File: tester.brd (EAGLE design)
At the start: 56 x 67 mm, 71 parts, among them IC1 ATmega8/88/168, K1 NA 05W K, M1 SP6000C-180, P1 250, P2 10k lin, Q1 BC847CSMD, Q2 BC847CSMD, Q3 BC328-40, Q4 8,000 MHz, Q5 BC847CSMD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

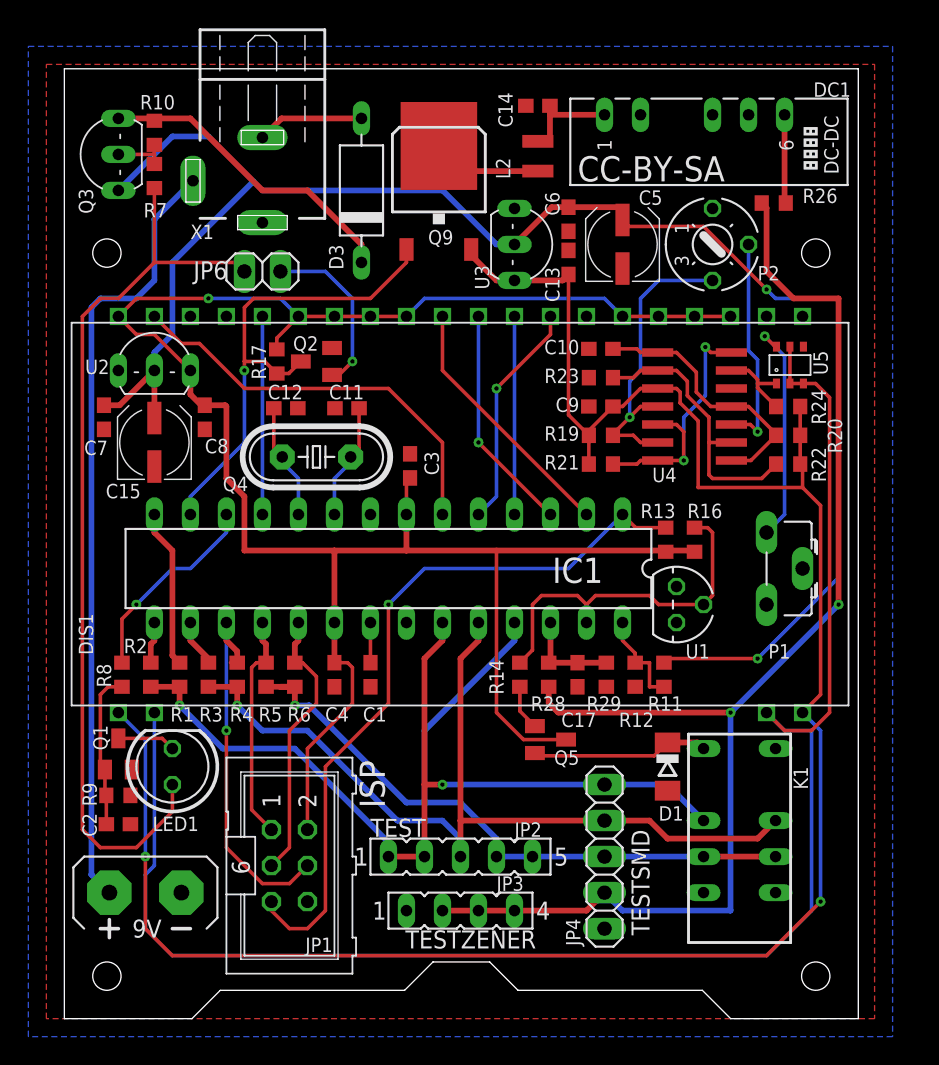
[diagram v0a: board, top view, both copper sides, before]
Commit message: rearranged top mask
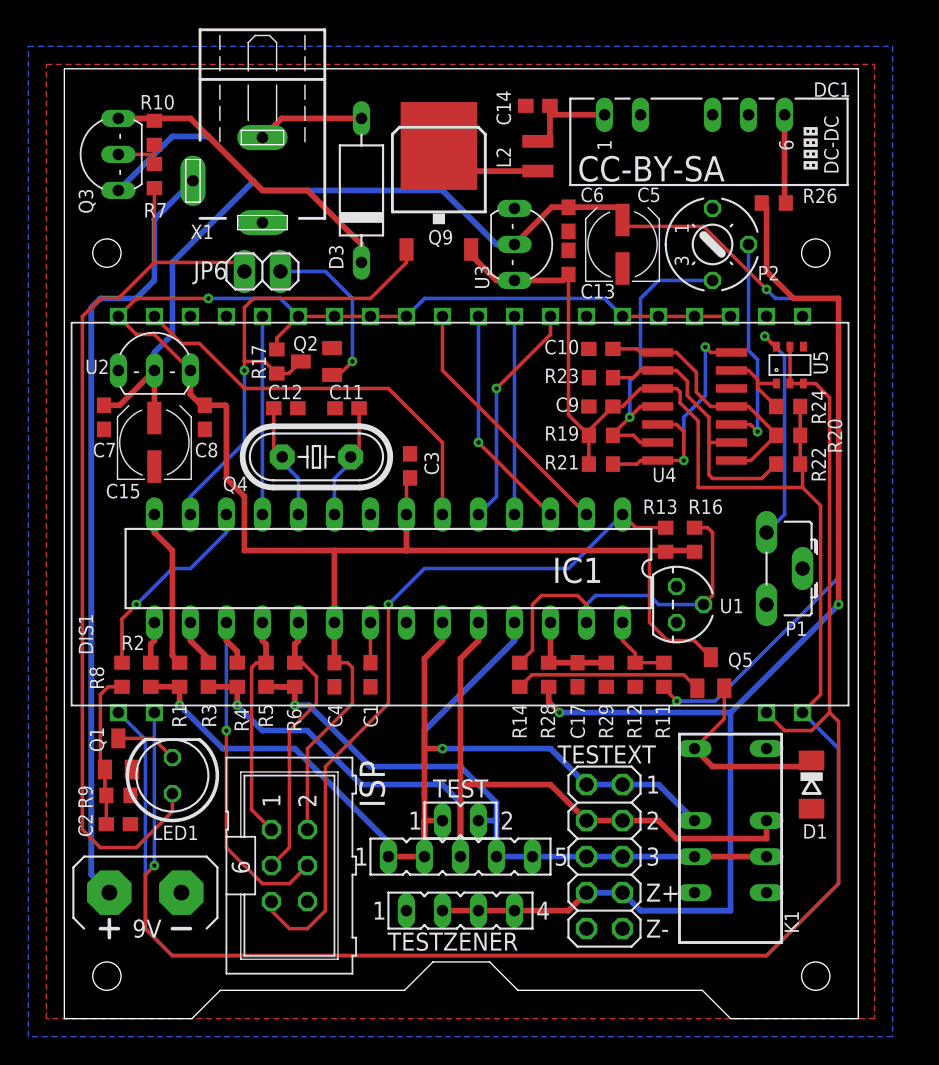
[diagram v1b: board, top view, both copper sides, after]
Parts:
- added JP7: TEST2, con-lsta:FE02-1
- JP4: value TESTSMD -> TESTEXT; device pinhead:1X05 -> pinhead:2X05
- JP6: value (none) -> POWERSW
- moved Q5 12.3 mm to (45.6, 24.4), turned to 0 degrees
- moved D1 10.2 mm to (52.7, 16.5)
- moved LED1 0.64 mm to (7.62, 17.1)
- moved K1 0.63 mm to (47.0, 12.7)
- turned R11 to 90 degrees
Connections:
- net +30V: now also JP4.7, JP4.8; no longer JP4.4
- net GND: now also JP4.10, JP4.9; no longer JP4.5
- net PC0: now also JP4.2, JP7.1
- net PC1: now also JP4.3, JP4.4; no longer JP4.2
- net PC2: now also JP4.5, JP4.6, JP7.2; no longer JP4.3
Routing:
- net N$22: track 3.21 -> 13.3 mm
- net +5V: track 146.9 -> 140.2 mm
- net PC0: track 63.4 -> 67.6 mm
- net PC1: track 64.6 -> 67.2 mm
- net N$23: track 12.5 -> 14.3 mm
- net PC5: track 6.93 -> 5.23 mm
- net V+: track 118.6 -> 120.1 mm
- net N$18: track 114.5 -> 113.1 mm, vias 0 -> 1
- net +5V/2: track 147.7 -> 148.7 mm, vias 2 -> 0
- net N$21: track 64.5 -> 63.9 mm
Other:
- board text added: "1"
- board text added: "2"
- board text added: "3"
- board text added: "Z+"
- board text added: "Z-"

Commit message: cleaned up some capacitor values, changed P2 to available pinout type
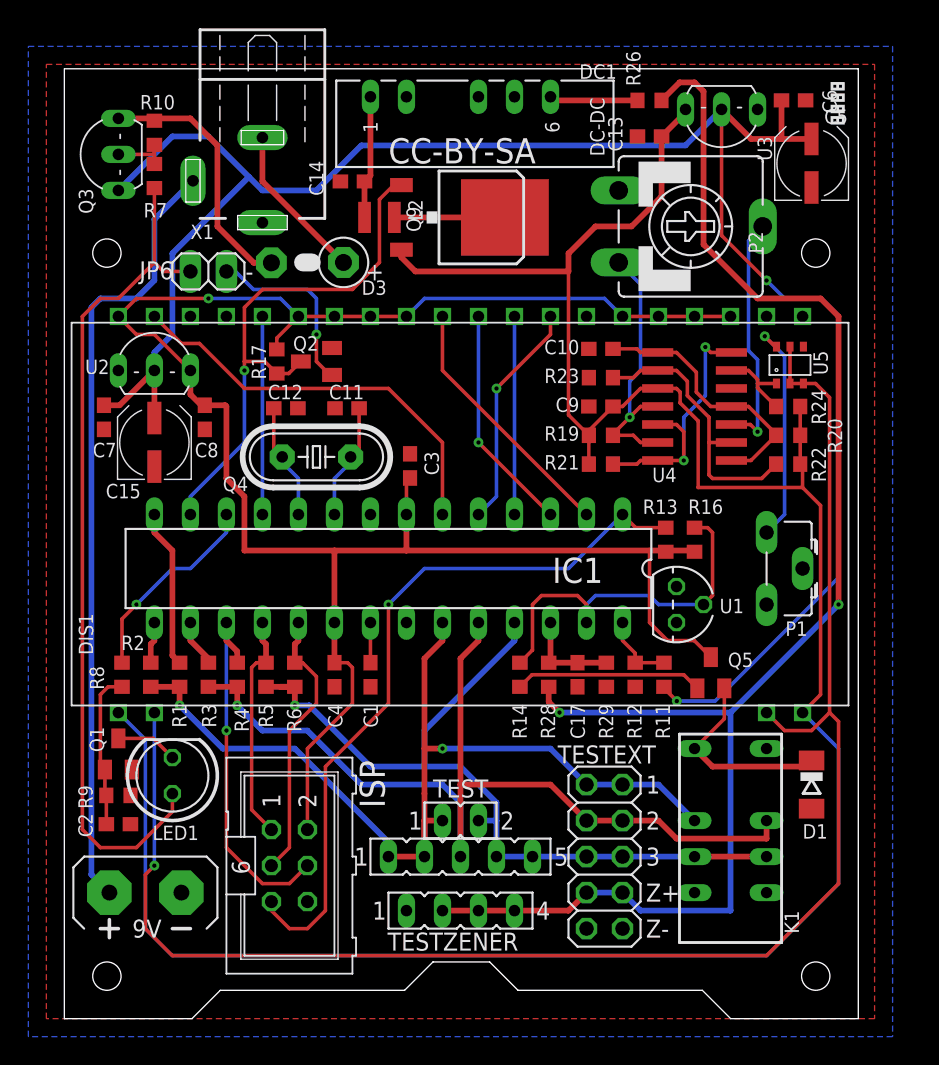
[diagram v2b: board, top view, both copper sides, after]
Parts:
- C1: value 1nF -> 1n
- C11, C12: value 22pF -> 22p
- C3, C4: value 100nF -> 100n
- D3: device markus:DIODE-3-10 -> markus:DIODE-3-5A-V
- P2: device pot:S75P -> pot:CA9V
- moved C6 18.0 mm to (51.4, 64.8), turned to 0 degrees
- moved U3 17.2 mm to (45.1, 64.1), turned to 180 degrees
- moved DC1 16.6 mm to (27.9, 65.0)
- moved C5 14.5 mm to (52.7, 60.3)
- moved C14 14.1 mm to (20.3, 59.1)
- moved L2 12.0 mm to (22.2, 56.5), turned to 180 degrees
- moved R26 11.4 mm to (41.3, 64.8), turned to 0 degrees
- moved C13 10.6 mm to (41.3, 62.2), turned to 180 degrees
- moved D3 6.35 mm to (17.1, 53.3), turned to 180 degrees
- moved JP6 3.81 mm to (10.2, 52.7)
- moved PLATINENSAMMLER 3.70 mm to (55.2, 62.9)
- moved Q9 3.33 mm to (28.6, 56.5), turned to 270 degrees
- moved P2 2.00 mm to (44.2, 55.9)
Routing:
- net +5V/2: track 148.7 -> 169.9 mm
- net V+: track 120.1 -> 136.7 mm
- net +30V: track 92.9 -> 106.9 mm
- net N$21: track 63.9 -> 60.1 mm
- net N$5: track 22.3 -> 18.5 mm
- net N$11: track 7.54 -> 11.2 mm
- net PD7: track 34.5 -> 38.1 mm
- net N$15: track 21.7 -> 19.3 mm
- net N$16: track 15.5 -> 17.2 mm
- net N$3: track 12.1 -> 13.6 mm
- net N$25: track 7.84 -> 8.69 mm

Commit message: switched lcd wiring to streifenraster
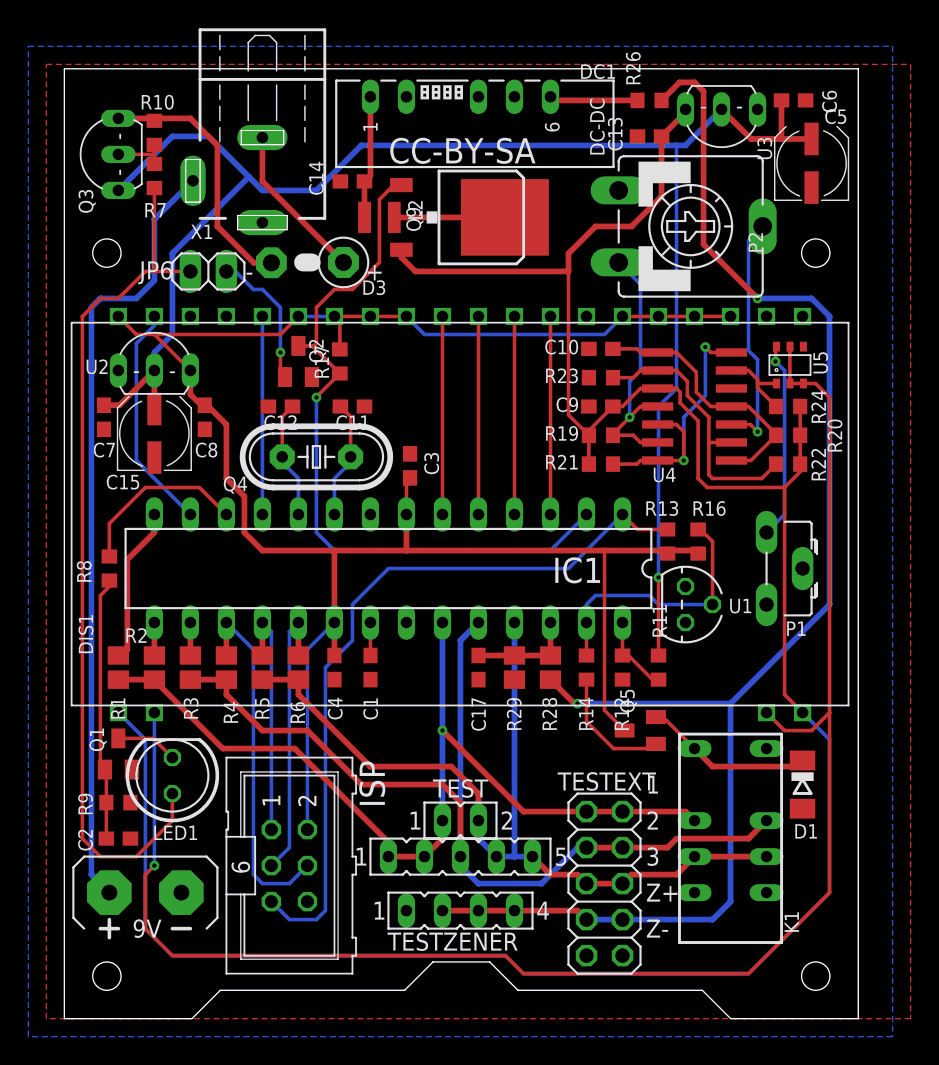
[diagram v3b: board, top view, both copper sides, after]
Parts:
- R1, R2, R28, R29, R3, R4, R5, R6: device resistor:R0603 -> resistor:R0805
- moved PLATINENSAMMLER 27.1 mm to (28.3, 66.0), turned to 180 degrees
- moved R8 7.55 mm to (3.17, 31.8)
- moved C17 7.00 mm to (29.2, 24.8)
- moved R29 6.50 mm to (31.8, 24.8)
- moved Q5 6.43 mm to (40.6, 20.3), turned to 90 degrees
- moved R14 4.73 mm to (36.8, 24.8)
- moved R17 4.45 mm to (19.4, 46.4)
- moved R1 4.35 mm to (3.81, 24.8)
- moved JP4 1.90 mm to (38.1, 9.53)
- moved R3 1.37 mm to (8.89, 24.8)
- moved Q2 1.27 mm to (16.5, 46.4), turned to 0 degrees
- moved R12 1.02 mm to (39.4, 24.8)
- moved C2 1.02 mm to (3.81, 12.7)
- moved R4 0.92 mm to (11.4, 24.8)
- moved R11 0.63 mm to (41.9, 24.8), turned to 270 degrees
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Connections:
- net PD0: now also Q2.3, Q9.1, R17.1; no longer DIS1.31
- net PD1: now also DIS1.28; no longer DIS1.30
- net PD3: now also DIS1.30; no longer DIS1.28
- net PD4: now also DIS1.31; no longer DIS1.39
- net PD7: now also DIS1.39; no longer Q2.3, Q9.1, R17.1
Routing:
- net PD0: track 18.2 -> 51.3 mm, vias 0 -> 1
- net PD7: track 38.1 -> 16.1 mm, vias 1 -> 0
- net V+: track 136.7 -> 118.2 mm, vias 2 -> 1
- net PD4: track 29.1 -> 14.0 mm
- net PC4: track 27.2 -> 18.8 mm
- net N$35: track 11.1 -> 18.6 mm
- net N$22: track 13.3 -> 8.78 mm
- net N$3: track 13.6 -> 9.90 mm
- net PC2: track 58.3 -> 61.3 mm, vias 1 -> 0
- net PC0: track 67.6 -> 64.8 mm, vias 2 -> 1
- net +30V: track 106.9 -> 104.2 mm
- net N$23: track 14.3 -> 12.0 mm
- net PD3: track 16.1 -> 14.0 mm, vias 1 -> 0
- net PD1: track 16.1 -> 14.0 mm, vias 1 -> 0
- net N$1: track 16.1 -> 14.0 mm
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
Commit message: power lcd bg led directly from v+
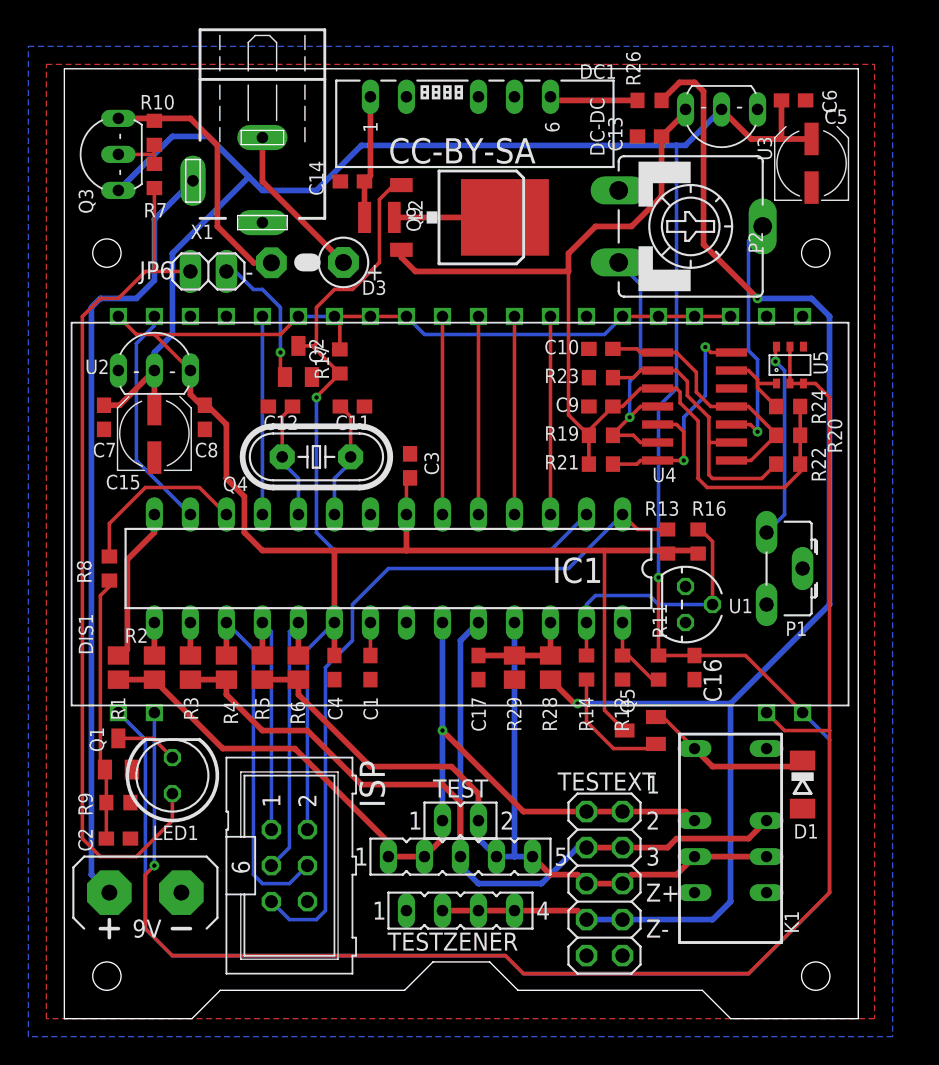
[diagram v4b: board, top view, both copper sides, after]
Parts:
- added C16: 100n, rcl:C0603
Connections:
- net +5V/2: no longer DIS1.1, DIS1.20
- net GND: now also C16.2
- net V+: now also C16.1, DIS1.1, DIS1.20
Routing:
- net +5V/2: track 168.7 -> 70.9 mm
- net V+: track 118.2 -> 211.5 mm
- net N$18: track 113.7 -> 113.1 mm
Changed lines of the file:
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@@
 <attribute name="VALUE" x="25.4" y="11.176" size="1.27" layer="27" ratio="10"/>
 </element>
+<element name="C16" library="rcl" package="C0603" value="100n" x="44.45" y="24.765" rot="R270"/>
 </elements>
 <signals>
@@
 <polygon width="0.254" layer="1" rank="2">
 <vertex x="-1.27" y="67.31"/>
-<vertex x="59.69" y="67.31"/>
-<vertex x="59.69" y="0"/>
+<vertex x="57.15" y="67.31"/>
+<vertex x="57.15" y="0"/>
 <vertex x="-1.27" y="0"/>
 </polygon>
@@
 <contactref element="IC1" pad="8"/>
 <contactref element="JP4" pad="10"/>
+<contactref element="C16" pad="2"/>
 <wire x1="48.895" y1="64.135" x2="52.285" y2="64.77" width="0" layer="19" extent="1-1"/>
 <wire x1="52.705" y1="58.625" x2="52.285" y2="64.77" width="0" layer="19" extent="1-1"/>
@@
 <wire x1="31.75" y1="23.915" x2="29.21" y2="23.915" width="0" layer="19" extent="1-1"/>
 <wire x1="39.37" y1="23.915" x2="31.75" y2="23.915" width="0" layer="19" extent="1-1"/>
-<wire x1="43.815" y1="27.94" x2="39.37" y2="23.915" width="0" layer="19" extent="1-1"/>
+<wire x1="44.45" y1="23.915" x2="39.37" y2="23.915" width="0" layer="19" extent="1-1"/>
+<wire x1="43.815" y1="27.94" x2="44.45" y2="23.915" width="0" layer="19" extent="1-1"/>
 <wire x1="49.53" y1="29.21" x2="43.815" y2="27.94" width="0" layer="19" extent="1-1"/>
 <wire x1="52.07" y1="31.75" x2="49.53" y2="29.21" width="0" layer="19" extent="1-1"/>
-<wire x1="49.53" y1="19.05" x2="49.53" y2="29.21" width="0" layer="19" extent="1-1"/>
+<wire x1="49.53" y1="19.05" x2="44.45" y2="23.915" width="0" layer="19" extent="1-1"/>
 <wire x1="52.07" y1="14.81" x2="49.53" y2="19.05" width="0" layer="19" extent="1-1"/>
 <wire x1="4.76" y1="17.569" x2="19.05" y2="23.915" width="0" layer="19" extent="1-1"/>
@@
 <wire x1="51.181" y1="47.401" x2="51.181" y2="44.801" width="0.254" layer="1"/>
 <wire x1="49.53" y1="21.59" x2="50.8" y2="20.32" width="0.254" layer="1"/>
-<wire x1="50.8" y1="20.32" x2="52.705" y2="20.32" width="0.254" layer="1"/>
-<wire x1="52.705" y1="20.32" x2="53.975" y2="21.59" width="0.254" layer="1"/>
-<wire x1="53.975" y1="21.59" x2="53.975" y2="43.815" width="0.254" layer="1"/>
+<wire x1="50.8" y1="20.32" x2="53.975" y2="20.32" width="0.254" layer="1"/>
+<wire x1="53.975" y1="20.32" x2="53.975" y2="43.815" width="0.254" layer="1"/>
 <wire x1="53.975" y1="8.89" x2="48.26" y2="3.175" width="0.254" layer="1"/>
 <wire x1="48.26" y1="3.175" x2="32.385" y2="3.175" width="0.254" layer="1"/>
@@
 <wire x1="52.989" y1="44.801" x2="52.131" y2="44.801" width="0.254" layer="1"/>
 <via x="6.35" y="10.795" extent="1-16" drill="0.3" shape="octagon"/>
-<wire x1="53.975" y1="8.89" x2="53.975" y2="21.59" width="0.254" layer="1"/>
+<wire x1="53.975" y1="8.89" x2="53.975" y2="20.32" width="0.254" layer="1"/>
 </signal>
 <signal name="+5V/2">
@@
 <contactref element="R24" pad="2"/>
 <contactref element="U4" pad="3"/>
-<contactref element="DIS1" pad="20"/>
-<contactref element="DIS1" pad="1"/>
 <wire x1="36.996" y1="39.116" x2="36.996" y2="41.148" width="0.254" layer="1"/>
 <wire x1="43.434" y1="43.434" x2="44.704" y2="42.164" width="0.254" layer="1"/>
@@
 <wire x1="38.696" y1="43.18" x2="36.996" y2="41.48" width="0.254" layer="1"/>
 <wire x1="36.996" y1="41.48" x2="36.996" y2="41.148" width="0.254" layer="1"/>
-<wire x1="52.07" y1="21.59" x2="50.8" y2="22.86" width="0.254" layer="1"/>
 <wire x1="51.904" y1="39.116" x2="51.982" y2="39.116" width="0.4064" layer="1"/>
 <wire x1="51.982" y1="39.116" x2="52.07" y2="39.204" width="0.4064" layer="1"/>
 <wire x1="35.56" y1="42.584" x2="36.996" y2="41.148" width="0.254" layer="1"/>
-<wire x1="7.62" y1="4.445" x2="31.115" y2="4.445" width="0.254" layer="16"/>
-<wire x1="31.115" y1="4.445" x2="32.385" y2="3.175" width="0.254" layer="16"/>
-<wire x1="32.385" y1="3.175" x2="48.26" y2="3.175" width="0.254" layer="16"/>
-<wire x1="48.26" y1="3.175" x2="53.975" y2="8.89" width="0.254" layer="16"/>
-<wire x1="3.81" y1="21.59" x2="5.715" y2="19.685" width="0.254" layer="16"/>
-<wire x1="5.715" y1="19.685" x2="5.715" y2="6.35" width="0.254" layer="16"/>
-<wire x1="5.715" y1="6.35" x2="7.62" y2="4.445" width="0.254" layer="16"/>
-<wire x1="52.07" y1="21.59" x2="53.975" y2="19.685" width="0.254" layer="16"/>
-<wire x1="53.975" y1="19.685" x2="53.975" y2="8.89" width="0.254" layer="16"/>
-<wire x1="50.8" y1="22.86" x2="50.8" y2="37.465" width="0.254" layer="1"/>
 <wire x1="50.8" y1="37.465" x2="45.339" y2="37.465" width="0.254" layer="1"/>
 <wire x1="45.339" y1="37.465" x2="44.704" y2="38.1" width="0.254" layer="1"/>
@@
 <wire x1="41.91" y1="43.18" x2="43.18" y2="44.45" width="0.254" layer="16"/>
 <wire x1="43.18" y1="44.45" x2="43.18" y2="61.595" width="0.254" layer="16"/>
+<contactref element="DIS1" pad="20"/>
+<contactref element="DIS1" pad="1"/>
+<wire x1="7.62" y1="4.445" x2="31.115" y2="4.445" width="0.254" layer="16"/>
+<wire x1="31.115" y1="4.445" x2="32.385" y2="3.175" width="0.254" layer="16"/>
+<wire x1="32.385" y1="3.175" x2="48.26" y2="3.175" width="0.254" layer="16"/>
+<wire x1="48.26" y1="3.175" x2="53.975" y2="8.89" width="0.254" layer="16"/>
+<wire x1="3.81" y1="21.59" x2="5.715" y2="19.685" width="0.254" layer="16"/>
+<wire x1="5.715" y1="19.685" x2="5.715" y2="6.35" width="0.254" layer="16"/>
+<wire x1="5.715" y1="6.35" x2="7.62" y2="4.445" width="0.254" layer="16"/>
+<wire x1="52.07" y1="21.59" x2="53.975" y2="19.685" width="0.254" layer="16"/>
+<wire x1="53.975" y1="19.685" x2="53.975" y2="8.89" width="0.254" layer="16"/>
+<wire x1="52.07" y1="21.59" x2="48.045" y2="25.615" width="0.254" layer="1"/>
+<wire x1="48.045" y1="25.615" x2="44.45" y2="25.615" width="0.254" layer="1"/>
+<contactref element="C16" pad="1"/>
+<wire x1="41.91" y1="25.615" x2="44.45" y2="25.615" width="0.254" layer="1"/>
 </signal>
 <signal name="N$1">
